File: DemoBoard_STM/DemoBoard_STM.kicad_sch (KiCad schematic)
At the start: 48 parts, among them J1 USB4110GFA, J2 Conn_ST_STDC14, J6 M55-7101242R, J7 MSD-1-A, J8 Conn_01x17_Pin, SW1 SW_Push, SW2 SW_Push, U1 STM32U375CGT6Q, U3 W25Q128JVPIQ TR, U4 TCAN332DCNR, U5 TLV75533PDBVR, Y1 32.768kHz, Y2 8Z-16.000MAHE-T

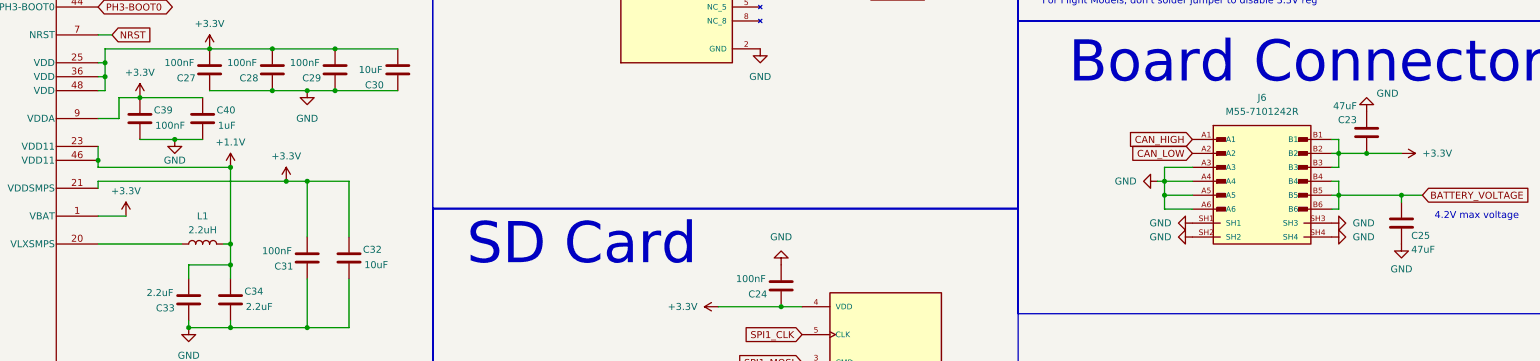
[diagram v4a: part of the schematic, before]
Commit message: Finalize STM payload + BOM
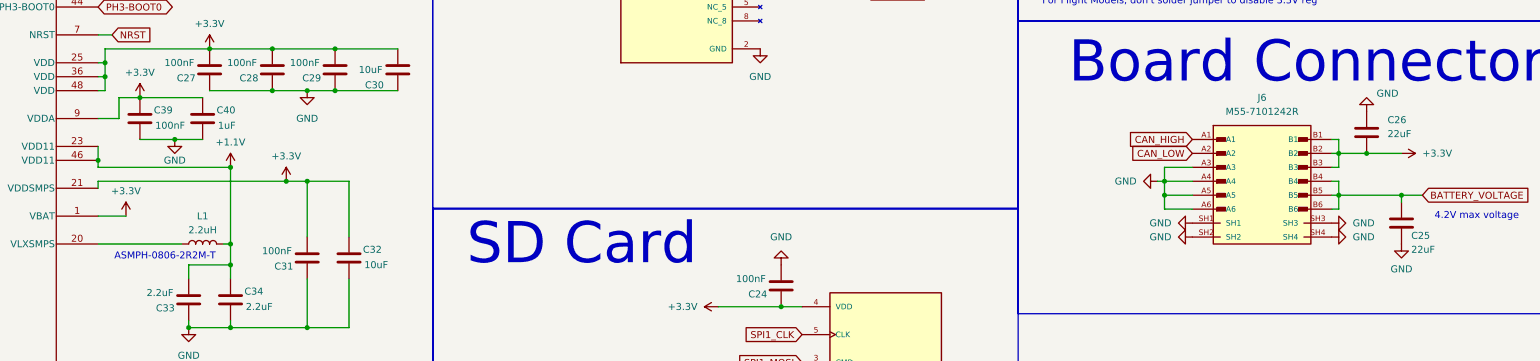
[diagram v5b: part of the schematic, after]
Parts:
- removed C23: 47uF, Capacitor_SMD:C_1206_3216Metric_Pad1.33x1.80mm_HandSolder, symbol Device:C
- added C26: 22uF, Capacitor_SMD:C_1210_3225Metric, symbol Device:C
- C18, C22, C30, C32: footprint Capacitor_SMD:C_0402_1005Metric_Pad0.74x0.62mm_HandSolder -> Capacitor_SMD:C_0603_1608Metric
- C25: value 47uF -> 22uF; footprint Capacitor_SMD:C_1206_3216Metric_Pad1.33x1.80mm_HandSolder -> Capacitor_SMD:C_1210_3225Metric
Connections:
- net +3.3V: now also C26.2
- net COVER_GND: now also C26.1
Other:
- note added: "ASMPH-0806-2R2M-T"
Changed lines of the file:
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@@
 		)
 	)
+	(text "ASMPH-0806-2R2M-T"
+		(exclude_from_sim no)
+		(at 139.192 108.966 0)
+		(effects
+			(font
+				(size 1.27 1.27)
+			)
+		)
+	)
 	(text "CAN Transceiver\n"
 		(exclude_from_sim no)
@@
 	)
 	(junction
+		(at 358.14 90.17)
+		(diameter 0)
+		(color 0 0 0 0)
+	)
+	(junction
 		(at 199.39 191.77)
 		(diameter 0)
@@
 	)
 	(junction
-		(at 358.14 90.17)
-		(diameter 0)
-		(color 0 0 0 0)
-	)
-	(junction
 		(at 55.88 124.46)
 		(diameter 0)
@@
 	(wire
 		(pts
-			(xy 364.49 90.17) (xy 358.14 90.17)
+			(xy 353.06 90.17) (xy 358.14 90.17)
 		)
 		(stroke
@@
 	(wire
 		(pts
-			(xy 358.14 90.17) (xy 353.06 90.17)
-		)
-		(stroke
-			(width 0)
-			(type default)
-		)
-	)
-	(wire
-		(pts
 			(xy 165.1 143.51) (xy 168.91 143.51)
 		)
@@
 	(wire
 		(pts
+			(xy 358.14 90.17) (xy 364.49 90.17)
+		)
+		(stroke
+			(width 0)
+			(type default)
+		)
+	)
+	(wire
+		(pts
 			(xy 130.81 83.82) (xy 130.81 80.01)
 		)
@@
 	)
 	(symbol
+		(lib_id "Device:C")
+		(at 358.14 86.36 0)
+		(unit 1)
+		(body_style 1)
+		(exclude_from_sim no)
+		(in_bom yes)
+		(on_board yes)
+		(in_pos_files yes)
+		(dnp no)
+		(property "Reference" "C26"
+			(at 361.95 84.074 0)
+			(show_name no)
+			(do_not_autoplace no)
+			(effects
+				(font
+					(size 1.27 1.27)
+				)
+				(justify left)
+			)
+		)
+		(property "Value" "22uF"
+			(at 361.95 86.614 0)
+			(show_name no)
+			(do_not_autoplace no)
+			(effects
+				(font
+					(size 1.27 1.27)
+				)
+				(justify left)
+			)
+		)
+		(property "Footprint" "Capacitor_SMD:C_1210_3225Metric"
+			(at 359.1052 90.17 0)
+			(hide yes)
+			(show_name no)
+			(do_not_autoplace no)
+			(effects
+				(font
+					(size 1.27 1.27)
+				)
+			)
+		)
+		(property "Datasheet" ""
+			(at 358.14 86.36 0)
+			(hide yes)
+			(show_name no)
+			(do_not_autoplace no)
+			(effects
+				(font
+					(size 1.27 1.27)
+				)
+			)
+		)
+		(property "Description" "Unpolarized capacitor"
+			(at 358.14 86.36 0)
+			(hide yes)
+			(show_name no)
+			(do_not_autoplace no)
+			(effects
+				(font
+					(size 1.27 1.27)
+				)
+			)
+		)
+		(pin "2"
+		)
+		(pin "1"
+		)
+		(instances
+			(project "DemoBoard_STM"
+				(path "/69f73f0f-32e5-40de-9ec6-e92a71672b5c"
+					(reference "C26")
+					(unit 1)
+				)
+			)
+		)
+	)
+	(symbol
 		(lib_id "power:GND")
 		(at 172.72 57.15 0)
@@
 			)
 		)
-		(property "Value" "47uF"
+		(property "Value" "22uF"
 			(at 366.268 107.696 0)
 			(show_name no)
@@
 			)
 		)
-		(property "Footprint" "Capacitor_SMD:C_1206_3216Metric_Pad1.33x1.80mm_HandSolder"
+		(property "Footprint" "Capacitor_SMD:C_1210_3225Metric"
 			(at 365.4552 106.68 0)
 			(hide yes)
@@
 			)
 		)
-		(property "Footprint" "Capacitor_SMD:C_0402_1005Metric_Pad0.74x0.62mm_HandSolder"
+		(property "Footprint" "Capacitor_SMD:C_0603_1608Metric"
 			(at 180.6448 71.12 0)
 			(hide yes)
@@
 			)
 		)
-		(property "Footprint" "Capacitor_SMD:C_0402_1005Metric_Pad0.74x0.62mm_HandSolder"
+		(property "Footprint" "Capacitor_SMD:C_0603_1608Metric"
 			(at 173.6852 113.03 0)
 			(hide yes)
@@
 			)
 		)
-		(property "Footprint" "Capacitor_SMD:C_0402_1005Metric_Pad0.74x0.62mm_HandSolder"
+		(property "Footprint" "Capacitor_SMD:C_0603_1608Metric"
 			(at 384.5052 44.45 0)
 			(hide yes)
@@
 			)
 		)
-		(property "Footprint" "Capacitor_SMD:C_0402_1005Metric_Pad0.74x0.62mm_HandSolder"
+		(property "Footprint" "Capacitor_SMD:C_0603_1608Metric"
 			(at 315.2648 39.37 0)
 			(hide yes)
@@
 					(unit 1)
 				)
-			)
-		)
-	)
-	(symbol
-		(lib_id "Device:C")
-		(at 358.14 86.36 180)
-		(unit 1)
-		(body_style 1)
-		(exclude_from_sim no)
-		(in_bom yes)
-		(on_board yes)
-		(in_pos_files yes)
-		(dnp no)
-		(property "Reference" "C23"
-			(at 356.362 84.074 0)
-			(show_name no)
-			(do_not_autoplace no)
-			(effects
-				(font
-					(size 1.27 1.27)
-				)
-				(justify left)
-			)
-		)
-		(property "Value" "47uF"
-			(at 356.362 81.534 0)
-			(show_name no)
-			(do_not_autoplace no)
-			(effects
-				(font
-					(size 1.27 1.27)
-				)
-				(justify left)
-			)
-		)
-		(property "Footprint" "Capacitor_SMD:C_1206_3216Metric_Pad1.33x1.80mm_HandSolder"
-			(at 357.1748 82.55 0)
-			(hide yes)
-			(show_name no)
-			(do_not_autoplace no)
-			(effects
-				(font
-					(size 1.27 1.27)
-				)
-			)
-		)
-		(property "Datasheet" ""
-			(at 358.14 86.36 0)
-			(hide yes)
-			(show_name no)
-			(do_not_autoplace no)
-			(effects
-				(font
-					(size 1.27 1.27)
-				)
-			)
-		)
-		(property "Description" "Unpolarized capacitor"
-			(at 358.14 86.36 0)
-			(hide yes)
-			(show_name no)
-			(do_not_autoplace no)
-			(effects
-				(font
-					(size 1.27 1.27)
-				)
-			)
-		)
-		(pin "2"
-		)
-		(pin "1"
-		)
-		(instances
-			(project "DemoBoard_STM"
-				(path "/69f73f0f-32e5-40de-9ec6-e92a71672b5c"
-					(reference "C23")
-					(unit 1)
-				)
